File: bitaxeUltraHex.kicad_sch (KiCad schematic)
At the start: 2 parts, among them J1 Conn_01x01, J2 Conn_01x01

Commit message: Resolved all unconnected pins, re-annotated, reviewed for layout
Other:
- sheet BM1366-3 ports: added none; removed CLKO, CO, NRSTO, RI
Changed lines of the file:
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@@
     (instances
       (project "bitaxeUltraHex"
-        (path "/e63e39d7-6ac0-4ffd-8aa3-1841a4541b55" (page "4"))
+        (path "/e63e39d7-6ac0-4ffd-8aa3-1841a4541b55" (page "5"))
       )
     )
@@
     (instances
       (project "bitaxeUltraHex"
-        (path "/e63e39d7-6ac0-4ffd-8aa3-1841a4541b55" (page "5"))
+        (path "/e63e39d7-6ac0-4ffd-8aa3-1841a4541b55" (page "4"))
       )
     )
@@
       (effects (font (size 1.27 1.27)) (justify left))
     )
-    (pin "NRSTO" output (at 218.44 85.725 0)
-      (effects (font (size 1.27 1.27)) (justify right))
-    )
-    (pin "CO" output (at 218.44 88.265 0)
-      (effects (font (size 1.27 1.27)) (justify right))
-    )
-    (pin "CLKO" output (at 218.44 93.345 0)
-      (effects (font (size 1.27 1.27)) (justify right))
-    )
-    (pin "RI" input (at 218.44 90.805 0)
-      (effects (font (size 1.27 1.27)) (justify right))
-    )
-    (instances
+    (instances

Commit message: add screw terminals, replace OLED display with optional connector
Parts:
- J1, J2: footprint bitaxe:63862-1 -> bitaxe:7770-screw-terminal
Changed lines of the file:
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@@
       (effects (font (size 1.27 1.27)) hide)
     )
-    (property "Footprint" "bitaxe:63862-1" (at 32.385 38.1 0)
+    (property "Footprint" "bitaxe:7770-screw-terminal" (at 32.385 38.1 0)
       (effects (font (size 1.27 1.27)) hide)
     )
@@
       (effects (font (size 1.27 1.27)) hide)
     )
-    (property "Footprint" "bitaxe:63862-1" (at 32.385 45.72 0)
+    (property "Footprint" "bitaxe:7770-screw-terminal" (at 32.385 45.72 0)
       (effects (font (size 1.27 1.27)) hide)
     )

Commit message: major rework of the power supply section
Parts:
- J1: value Conn_01x01 -> Screw Terminal; DK A100886CT-ND -> 36-7770-ND; PARTNO 63862-1 -> 36-7770
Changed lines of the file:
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@@
       (effects (font (size 1.27 1.27)))
     )
-    (property "Value" "Conn_01x01" (at 32.385 34.29 0)
+    (property "Value" "Screw Terminal" (at 32.385 34.29 0)
       (effects (font (size 1.27 1.27)) hide)
     )
@@
       (effects (font (size 1.27 1.27)) hide)
     )
-    (property "Datasheet" "https://www.te.com/commerce/DocumentDelivery/DDEController?Action=srchrtrv&DocNm=63862&DocType=Customer+Drawing&DocLang=English" (at 32.385 38.1 0)
+    (property "Datasheet" "https://mm.digikey.com/Volume0/opasdata/d220001/medias/docus/581/Metric_PCB_Screw_Terminals.pdf" (at 32.385 38.1 0)
       (effects (font (size 1.27 1.27)) hide)
     )
-    (property "DK" "A100886CT-ND" (at 32.385 38.1 0)
+    (property "DK" "36-7770-ND" (at 32.385 38.1 0)
       (effects (font (size 1.27 1.27)) hide)
     )
-    (property "PARTNO" "63862-1" (at 32.385 38.1 0)
+    (property "PARTNO" "36-7770" (at 32.385 38.1 0)
       (effects (font (size 1.27 1.27)) hide)
     )

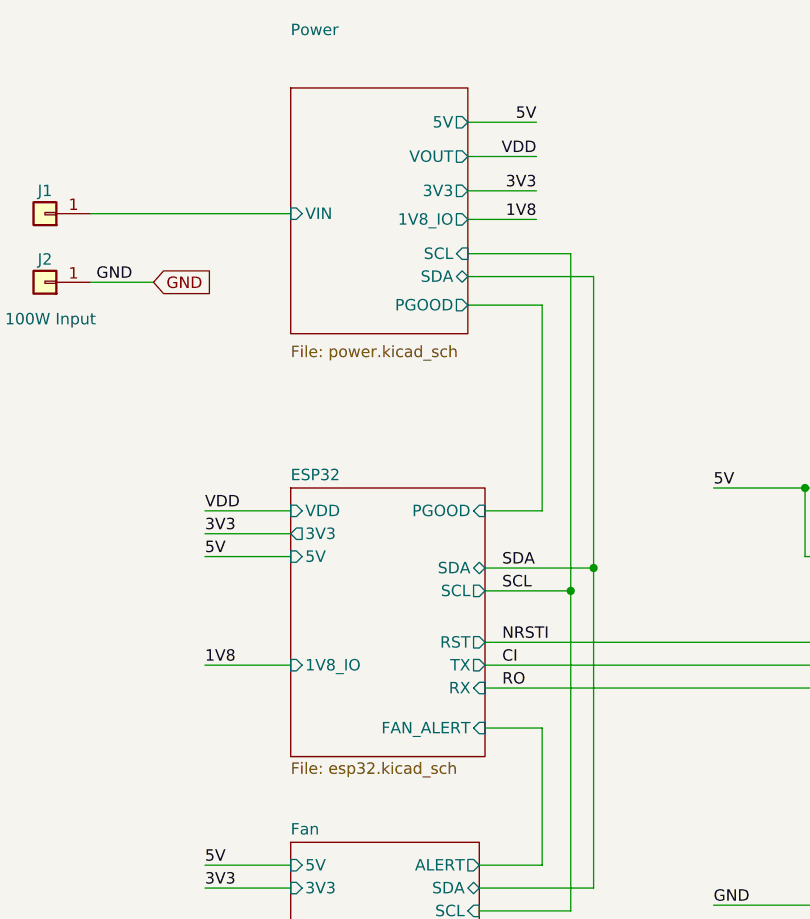
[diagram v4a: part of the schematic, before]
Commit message: added PWR_EN transistor
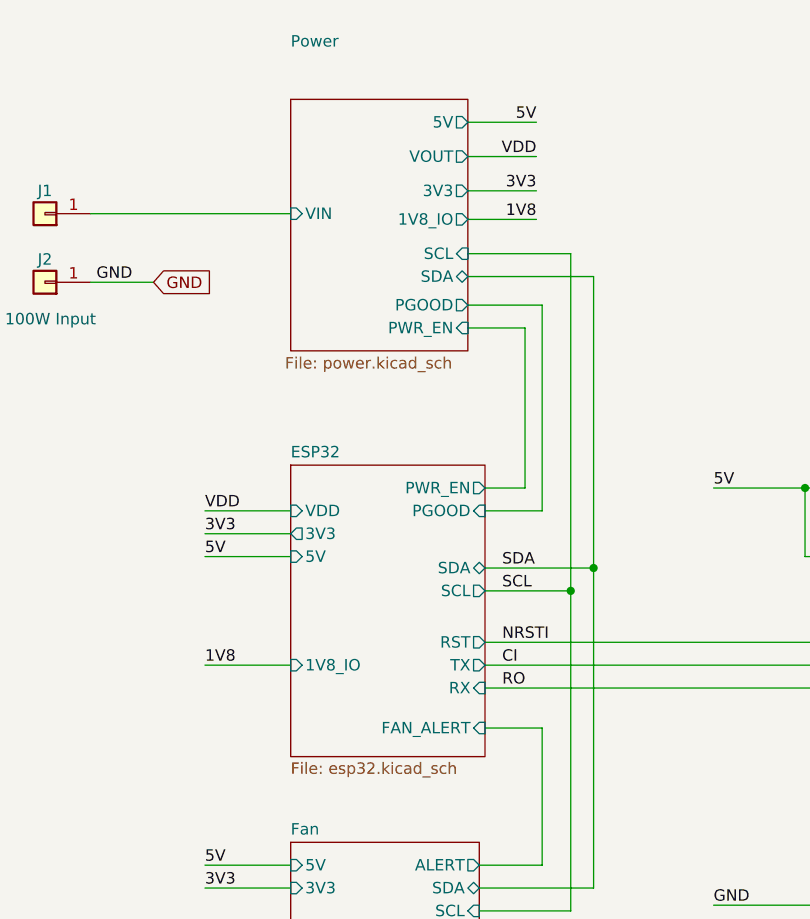
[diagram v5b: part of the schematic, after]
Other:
- sheet ESP32 ports: added PWR_EN; removed none
- sheet Power ports: added PWR_EN; removed none
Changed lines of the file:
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@@
+    (stroke (width 0) (type default))
+  )
+  (wire (pts (xy 85.725 50.8) (xy 79.375 50.8))
     (stroke (width 0) (type default))
   )
@@
     (stroke (width 0) (type default))
   )
+  (wire (pts (xy 81.28 68.58) (xy 85.725 68.58))
+    (stroke (width 0) (type default))
+  )
   (wire (pts (xy 154.94 99.06) (xy 154.94 114.935))
     (stroke (width 0) (type default))
@@
   )
   (wire (pts (xy 79.375 35.56) (xy 86.995 35.56))
+    (stroke (width 0) (type default))
+  )
+  (wire (pts (xy 85.725 68.58) (xy 85.725 50.8))
     (stroke (width 0) (type default))
   )
@@
     )
   )
-  (sheet (at 59.69 24.13) (size 19.685 27.305)
+  (sheet (at 59.69 25.4) (size 19.685 27.94)
     (stroke (width 0.1524) (type solid))
     (fill (color 255 255 194 1.0000))
-    (property "Sheetname" "Power" (at 59.69 18.415 0)
+    (property "Sheetname" "Power" (at 59.69 19.685 0)
       (effects (font (size 1.27 1.27)) (justify left bottom))
     )
-    (property "Sheetfile" "power.kicad_sch" (at 59.69 52.705 0)
+    (property "Sheetfile" "power.kicad_sch" (at 59.055 53.975 0)
       (effects (font (size 1.27 1.27)) (justify left top))
     )
@@
       (effects (font (size 1.27 1.27)) (justify right))
     )
+    (pin "PWR_EN" input (at 79.375 50.8 0)
+      (effects (font (size 1.27 1.27)) (justify right))
+    )
     (instances
       (project "bitaxeUltraHex"
@@
     )
   )
-  (sheet (at 59.69 68.58) (size 21.59 29.845) (fields_autoplaced)
+  (sheet (at 59.69 66.04) (size 21.59 32.385) (fields_autoplaced)
     (stroke (width 0.1524) (type solid))
     (fill (color 255 255 194 1.0000))
-    (property "Sheetname" "ESP32" (at 59.69 67.8684 0)
+    (property "Sheetname" "ESP32" (at 59.69 65.3284 0)
       (effects (font (size 1.27 1.27)) (justify left bottom))
     )
@@
       (effects (font (size 1.27 1.27)) (justify left))
     )
-    (instances
+    (pin "PWR_EN" output (at 81.28 68.58 0)
+      (effects (font (size 1.27 1.27)) (justify right))
+    )
+    (instances

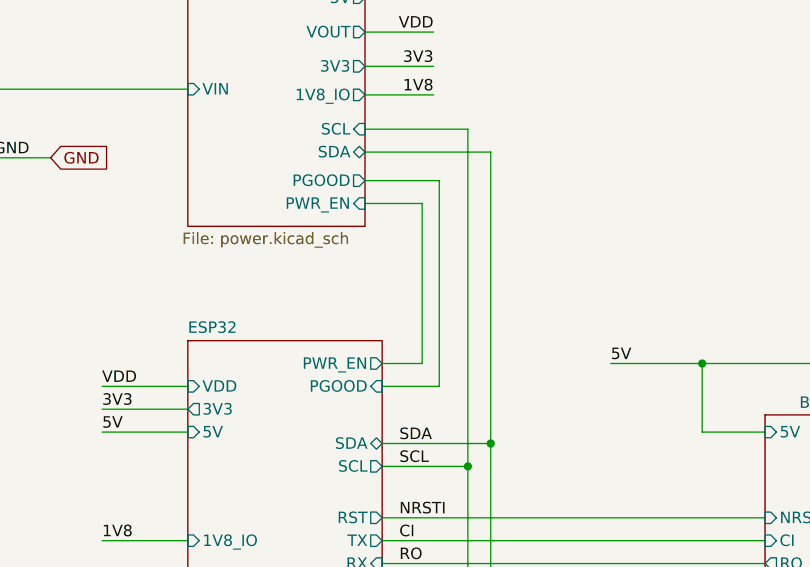
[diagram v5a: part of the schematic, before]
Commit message: switched PWR_EN to GPIO10 so that we can match this up better with ultra-v1.2
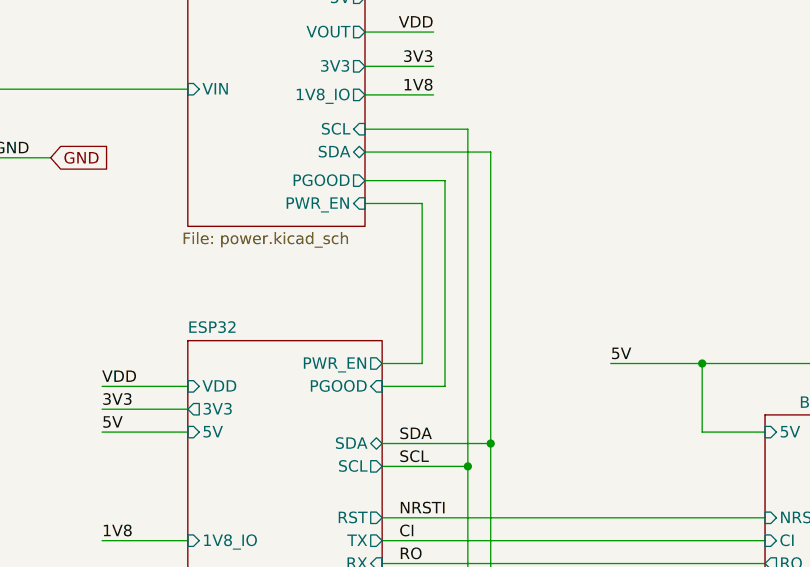
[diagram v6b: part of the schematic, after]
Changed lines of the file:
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@@
     (stroke (width 0) (type default))
   )
-  (wire (pts (xy 87.63 48.26) (xy 87.63 71.12))
+  (wire (pts (xy 88.265 48.26) (xy 88.265 71.12))
     (stroke (width 0) (type default))
   )
@@
     (stroke (width 0) (type default))
   )
-  (wire (pts (xy 79.375 48.26) (xy 87.63 48.26))
+  (wire (pts (xy 79.375 48.26) (xy 88.265 48.26))
     (stroke (width 0) (type default))
   )
-  (wire (pts (xy 87.63 71.12) (xy 81.28 71.12))
+  (wire (pts (xy 88.265 71.12) (xy 81.28 71.12))
     (stroke (width 0) (type default))
   )

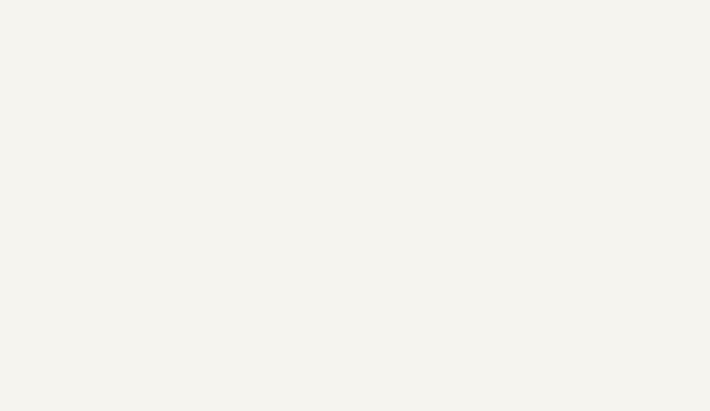
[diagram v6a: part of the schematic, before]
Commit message: added fiducials
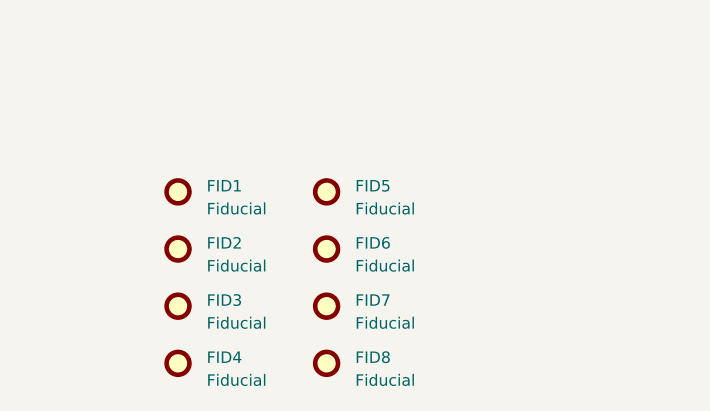
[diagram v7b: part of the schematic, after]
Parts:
- added FID1, FID2, FID3, FID4, FID5, FID6, FID7, FID8: Fiducial, Fiducial:Fiducial_1mm_Mask2mm, symbol Mechanical:Fiducial
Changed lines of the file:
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@@
+    )
+  )
+  (symbol (lib_id "Mechanical:Fiducial") (at 53.975 172.085 0) (unit 1)
+    (in_bom no) (on_board yes) (dnp no) (fields_autoplaced)
+    (property "Reference" "FID5" (at 57.15 171.45 0)
+      (effects (font (size 1.27 1.27)) (justify left))
+    )
+    (property "Value" "Fiducial" (at 57.15 173.99 0)
+      (effects (font (size 1.27 1.27)) (justify left))
+    )
+    (property "Footprint" "Fiducial:Fiducial_1mm_Mask2mm" (at 53.975 172.085 0)
+      (effects (font (size 1.27 1.27)) hide)
+    )
+    (property "Datasheet" "~" (at 53.975 172.085 0)
+      (effects (font (size 1.27 1.27)) hide)
+    )
+    (instances
+      (project "bitaxeUltraHex"
+        (path "/e63e39d7-6ac0-4ffd-8aa3-1841a4541b55"
+          (reference "FID5") (unit 1)
+        )
+      )
     )
   )
@@
         (path "/e63e39d7-6ac0-4ffd-8aa3-1841a4541b55"
           (reference "#G1") (unit 1)
+        )
+      )
+    )
+  )
+  (symbol (lib_id "Mechanical:Fiducial") (at 53.975 178.435 0) (unit 1)
+    (in_bom no) (on_board yes) (dnp no) (fields_autoplaced)
+    (property "Reference" "FID6" (at 57.15 177.8 0)
+      (effects (font (size 1.27 1.27)) (justify left))
+    )
+    (property "Value" "Fiducial" (at 57.15 180.34 0)
+      (effects (font (size 1.27 1.27)) (justify left))
+    )
+    (property "Footprint" "Fiducial:Fiducial_1mm_Mask2mm" (at 53.975 178.435 0)
+      (effects (font (size 1.27 1.27)) hide)
+    )
+    (property "Datasheet" "~" (at 53.975 178.435 0)
+      (effects (font (size 1.27 1.27)) hide)
+    )
+    (instances
+      (project "bitaxeUltraHex"
+        (path "/e63e39d7-6ac0-4ffd-8aa3-1841a4541b55"
+          (reference "FID6") (unit 1)
+        )
+      )
+    )
+  )
+  (symbol (lib_id "Mechanical:Fiducial") (at 53.975 184.785 0) (unit 1)
+    (in_bom no) (on_board yes) (dnp no) (fields_autoplaced)
+    (property "Reference" "FID7" (at 57.15 184.15 0)
+      (effects (font (size 1.27 1.27)) (justify left))
+    )
+    (property "Value" "Fiducial" (at 57.15 186.69 0)
+      (effects (font (size 1.27 1.27)) (justify left))
+    )
+    (property "Footprint" "Fiducial:Fiducial_1mm_Mask2mm" (at 53.975 184.785 0)
+      (effects (font (size 1.27 1.27)) hide)
+    )
+    (property "Datasheet" "~" (at 53.975 184.785 0)
+      (effects (font (size 1.27 1.27)) hide)
+    )
+    (instances
+      (project "bitaxeUltraHex"
+        (path "/e63e39d7-6ac0-4ffd-8aa3-1841a4541b55"
+          (reference "FID7") (unit 1)
         )
       )
@@
         )
       )
+    )
+  )
+  (symbol (lib_id "Mechanical:Fiducial") (at 37.465 184.785 0) (unit 1)
+    (in_bom no) (on_board yes) (dnp no) (fields_autoplaced)
+    (property "Reference" "FID3" (at 40.64 184.15 0)
+      (effects (font (size 1.27 1.27)) (justify left))
+    )
+    (property "Value" "Fiducial" (at 40.64 186.69 0)
+      (effects (font (size 1.27 1.27)) (justify left))
+    )
+    (property "Footprint" "Fiducial:Fiducial_1mm_Mask2mm" (at 37.465 184.785 0)
+      (effects (font (size 1.27 1.27)) hide)
+    )
+    (property "Datasheet" "~" (at 37.465 184.785 0)
+      (effects (font (size 1.27 1.27)) hide)
+    )
+    (instances
+      (project "bitaxeUltraHex"
+        (path "/e63e39d7-6ac0-4ffd-8aa3-1841a4541b55"
+          (reference "FID3") (unit 1)
+        )
+      )
+    )
+  )
+  (symbol (lib_id "Mechanical:Fiducial") (at 53.975 191.135 0) (unit 1)
+    (in_bom no) (on_board yes) (dnp no) (fields_autoplaced)
+    (property "Reference" "FID8" (at 57.15 190.5 0)
+      (effects (font (size 1.27 1.27)) (justify left))
+    )
+    (property "Value" "Fiducial" (at 57.15 193.04 0)
+      (effects (font (size 1.27 1.27)) (justify left))
+    )
+    (property "Footprint" "Fiducial:Fiducial_1mm_Mask2mm" (at 53.975 191.135 0)
+      (effects (font (size 1.27 1.27)) hide)
+    )
+    (property "Datasheet" "~" (at 53.975 191.135 0)
+      (effects (font (size 1.27 1.27)) hide)
+    )
+    (instances
+      (project "bitaxeUltraHex"
+        (path "/e63e39d7-6ac0-4ffd-8aa3-1841a4541b55"
+          (reference "FID8") (unit 1)
+        )
+      )
+    )
+  )
+  (symbol (lib_id "Mechanical:Fiducial") (at 37.465 178.435 0) (unit 1)
+    (in_bom no) (on_board yes) (dnp no) (fields_autoplaced)
+    (property "Reference" "FID2" (at 40.64 177.8 0)
+      (effects (font (size 1.27 1.27)) (justify left))
+    )
+    (property "Value" "Fiducial" (at 40.64 180.34 0)
+      (effects (font (size 1.27 1.27)) (justify left))
+    )
+    (property "Footprint" "Fiducial:Fiducial_1mm_Mask2mm" (at 37.465 178.435 0)
+      (effects (font (size 1.27 1.27)) hide)
+    )
+    (property "Datasheet" "~" (at 37.465 178.435 0)
+      (effects (font (size 1.27 1.27)) hide)
+    )
+    (instances
+      (project "bitaxeUltraHex"
+        (path "/e63e39d7-6ac0-4ffd-8aa3-1841a4541b55"
+          (reference "FID2") (unit 1)
+        )
+      )
+    )
+  )
+  (symbol (lib_id "Mechanical:Fiducial") (at 37.465 191.135 0) (unit 1)
+    (in_bom no) (on_board yes) (dnp no) (fields_autoplaced)
+    (property "Reference" "FID4" (at 40.64 190.5 0)
+      (effects (font (size 1.27 1.27)) (justify left))
+    )
+    (property "Value" "Fiducial" (at 40.64 193.04 0)
+      (effects (font (size 1.27 1.27)) (justify left))
+    )
+    (property "Footprint" "Fiducial:Fiducial_1mm_Mask2mm" (at 37.465 191.135 0)
+      (effects (font (size 1.27 1.27)) hide)
+    )
+    (property "Datasheet" "~" (at 37.465 191.135 0)
+      (effects (font (size 1.27 1.27)) hide)
+    )
+    (instances
+      (project "bitaxeUltraHex"
+        (path "/e63e39d7-6ac0-4ffd-8aa3-1841a4541b55"
+          (reference "FID4") (unit 1)
+        )
+      )
+    )
+  )
+  (symbol (lib_id "Mechanical:Fiducial") (at 37.465 172.085 0) (unit 1)
+    (in_bom no) (on_board yes) (dnp no) (fields_autoplaced)
+    (property "Reference" "FID1" (at 40.64 171.45 0)
+      (effects (font (size 1.27 1.27)) (justify left))
+    )
+    (property "Value" "Fiducial" (at 40.64 173.99 0)
+      (effects (font (size 1.27 1.27)) (justify left))
+    )
+    (property "Footprint" "Fiducial:Fiducial_1mm_Mask2mm" (at 37.465 172.085 0)
+      (effects (font (size 1.27 1.27)) hide)
+    )
+    (property "Datasheet" "~" (at 37.465 172.085 0)
+      (effects (font (size 1.27 1.27)) hide)
+    )
+    (instances
+      (project "bitaxeUltraHex"
+        (path "/e63e39d7-6ac0-4ffd-8aa3-1841a4541b55"
+          (reference "FID1") (unit 1)
+        )
+      )
